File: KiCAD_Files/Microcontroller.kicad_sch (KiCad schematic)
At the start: 33 parts, among them J403 RJE721881411, J404 RJE721881411, U401 OwnTech_SPIN, U402 TCAN334GDR

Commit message: Schematic close to completion.
Signed-off-by: Jean Alinei <jean.alinei@owntech.org>
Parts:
- C40: renamed from C401; LCSC (none) -> C5449000
- renumbered J403 to J12, J404 to J13, JP412 to JP1, JP413 to JP2, JP405 to JP3, JP406 to JP4, JP414 to JP5, JP415 to JP6, JP402 to JP7, JP401 to JP8, R421 to R12, R406 to R13, R407 to R14, R403 to R15, R405 to R16, R402 to R17, R404 to R18, R401 to R19, TH402 to TH1, TH401 to TH2, TP409 to TP1, TP408 to TP10, TP410 to TP2, TP401 to TP3, TP405 to TP4, TP402 to TP5, TP406 to TP6, TP403 to TP7, TP407 to TP8, TP404 to TP9, U401 to U3, U402 to U4

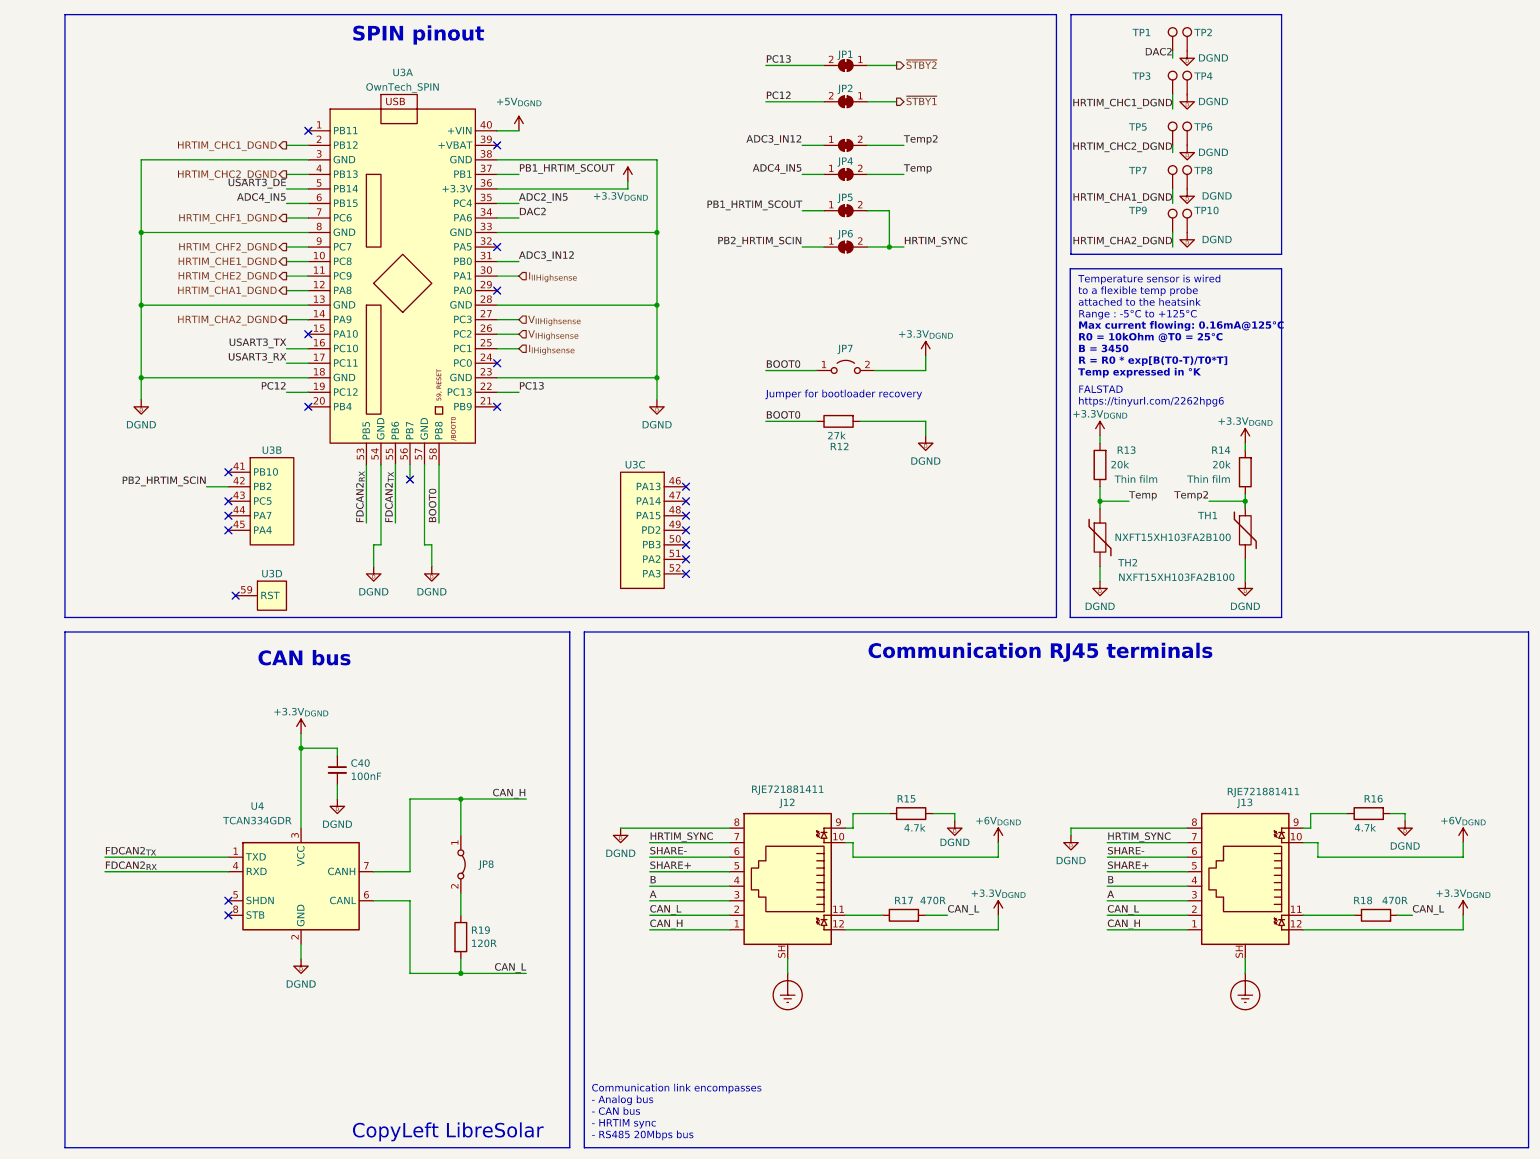
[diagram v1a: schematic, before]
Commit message: First routing pass complete.
Signed-off-by: Jean Alinei <jean.alinei@owntech.org>
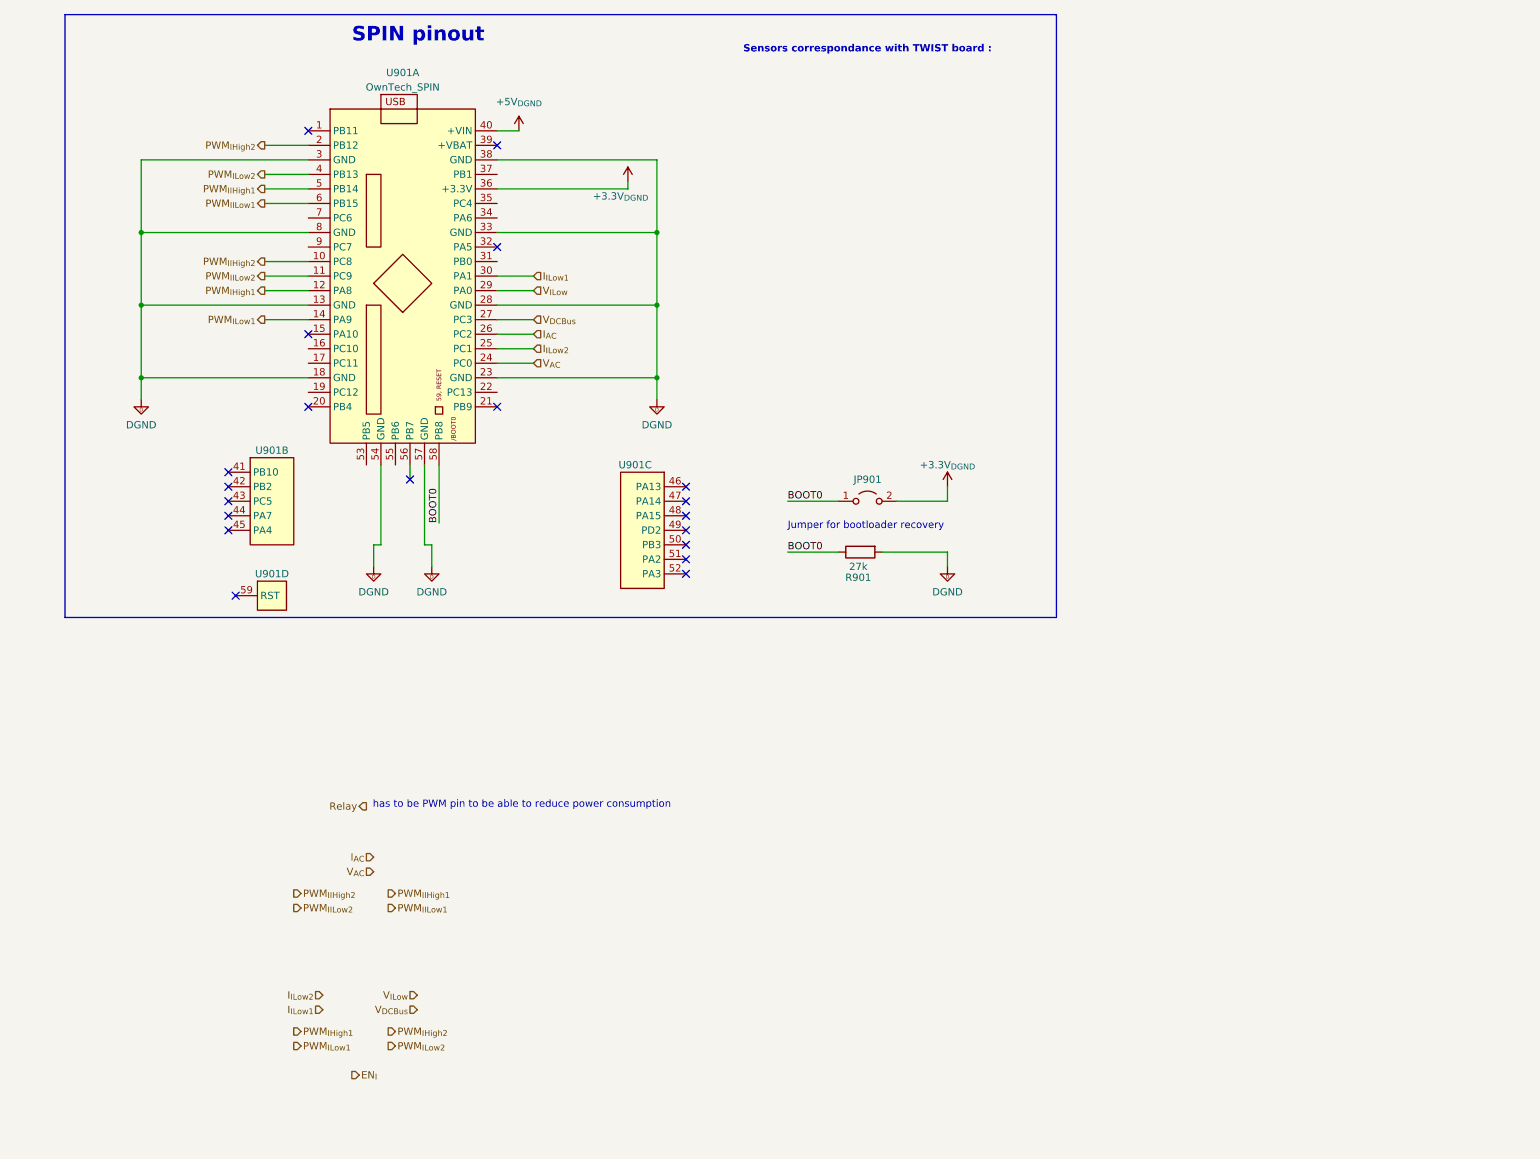
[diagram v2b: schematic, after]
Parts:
- removed C40: 100nF, Capacitor_SMD:C_1206_3216Metric, symbol Device:C_Small
- removed J12, J13: RJE721881411, Footprints:ethernet_RJE721881411, symbol Connector:RJ45_LED_Shielded
- removed JP1, JP2, JP4, JP5, JP6: Jumper_2_Bridged, Jumper:SolderJumper-2_P1.3mm_Bridged_RoundedPad1.0x1.5mm, symbol Jumper:SolderJumper_2_Bridged
- removed JP3: Jumper_2_Bridged, Jumper:SolderJumper-2_P1.3mm_Bridged_Pad1.0x1.5mm, symbol Jumper:SolderJumper_2_Bridged
- removed JP8: Jumper, Connector_PinHeader_2.54mm:PinHeader_1x02_P2.54mm_Vertical, symbol Jumper:Jumper_2_Bridged
- removed R13, R14: 20k, Footprints:R_0805_2012Metric, symbol Device:R
- removed R15, R16: 4.7k, Footprints:R_0805_2012Metric, symbol Device:R
- removed R17, R18: 470R, Footprints:R_0805_2012Metric, symbol Device:R
- removed R19: 120R, Footprints:R_0805_2012Metric, symbol Device:R
- removed TH1, TH2: NXFT15XH103FA2B100, Connector_PinHeader_2.00mm:PinHeader_1x02_P2.00mm_Vertical, symbol Device:Thermistor
- removed TP1, TP10, TP2, TP3, TP4, TP5, TP6, TP7, TP8, TP9: TestPoint, Footprints:TestPoint_THTPad_D1.5mm_Drill0.7mm, symbol Connector:TestPoint
- removed U4: TCAN334GDR, Footprints:SOIC-8_3.9x4.9mm_P1.27mm, symbol Interface_CAN_LIN:TCAN334
- U901: renamed from U3; footprint Footprints:OwnTech_SPINTHT -> Footprints:OwnTech_SPINTHT_1
- renumbered JP7 to JP901, R12 to R901
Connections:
- net V_{AC}: now reaches U901.24 (PC0)
- net V_{ILow}: now reaches U901.29 (PA0)
- net ADC2_IN5: no longer names the net of U901.35 (PC4)
- net ADC3_IN12: no longer names the net of U901.31 (PB0)
- net ADC4_IN5 renamed PWM_{IILow1}
- net DAC2: no longer names the net of U901.34 (PA6)
- net FDCAN2_{RX}: no longer names the net of U901.53 (PB5)
- net FDCAN2_{TX}: no longer names the net of U901.55 (PB6)
- net HRTIM_CHA1_DGND renamed PWM_{IHigh1}
- net HRTIM_CHA2_DGND renamed PWM_{ILow1}
- net HRTIM_CHC1_DGND renamed PWM_{IHigh2}
- net HRTIM_CHC2_DGND renamed PWM_{ILow2}
- net HRTIM_CHE1_DGND renamed PWM_{IIHigh2}
- net HRTIM_CHE2_DGND renamed PWM_{IILow2}
- net HRTIM_CHF1_DGND: no longer names the net of U901.7 (PC6)
- net HRTIM_CHF2_DGND: no longer names the net of U901.9 (PC7)
- net I_{IHighsense} renamed I_{ILow2}
- net I_{IIHighsense} renamed I_{ILow1}
- net PB1_HRTIM_SCOUT: no longer names the net of U901.37 (PB1)
- net PB2_HRTIM_SCIN: no longer names the net of U901.42 (PB2)
- net PC12: no longer names the net of U901.19 (PC12)
- net PC13: no longer names the net of U901.22 (PC13)
- net USART3_DE renamed PWM_{IIHigh1}
- net USART3_RX: no longer names the net of U901.17 (PC11)
- net USART3_TX: no longer names the net of U901.16 (PC10)
- net V_{IHighsense} renamed I_{AC}
- net V_{IIHighsense} renamed V_{DCBus}
- no-connect marks 23 -> 20
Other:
- note added: "Sensors correspondance with TWIST board :"
- note added: "has to be PWM pin to be able to reduce power consumption"
- note removed: "CAN bus"
- note removed: "Communication RJ45 terminals"
- note removed: "Communication link encompasses - Analog bus - CAN bus - HRTIM sync - RS485 20Mbps bus"
- note removed: "CopyLeft LibreSolar"
- note removed: "FALSTAD https://tinyurl.com/2262hpg6"
- note removed: "Max current flowing: 0.16mA@125°C R0 = 10kOhm @T0 = 25°C B = 3450 R = R0 * exp[B(T0-T)/T0*T] Temp expressed in °K"
- note removed: "Temperature sensor is wired to a flexible temp probe attached to the heatsink Range : -5°C to +125°C"
- moved on the sheet: JP901, R901

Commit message: Added missing tracks for sensors and relay. Fixed many routing issues.
Signed-off-by: Jean Alinei <jean.alinei@owntech.org>
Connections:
- net EN_{I}: now also U901.19 (PC12)
- net Relay: now also U901.22 (PC13)
- net DIS_{HV}: now reaches U901.21 (PB9)
- no-connect marks 20 -> 19
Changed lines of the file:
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@@
 	(rectangle
 		(start 23.495 15.24)
-		(end 196.85 120.65)
+		(end 229.87 120.65)
 		(stroke
 			(width 0)
@@
 	)
 	(no_connect
-		(at 99.06 83.82)
-	)
-	(no_connect
 		(at 132.08 105.41)
 	)
@@
 	(wire
 		(pts
+			(xy 99.06 81.28) (xy 105.41 81.28)
+		)
+		(stroke
+			(width 0)
+			(type default)
+		)
+	)
+	(wire
+		(pts
 			(xy 99.06 63.5) (xy 105.41 63.5)
 		)
@@
 	(wire
 		(pts
+			(xy 99.06 83.82) (xy 105.41 83.82)
+		)
+		(stroke
+			(width 0)
+			(type default)
+		)
+	)
+	(wire
+		(pts
 			(xy 58.42 63.5) (xy 66.04 63.5)
 		)
@@
 		(pts
 			(xy 58.42 58.42) (xy 66.04 58.42)
+		)
+		(stroke
+			(width 0)
+			(type default)
+		)
+	)
+	(wire
+		(pts
+			(xy 58.42 81.28) (xy 66.04 81.28)
 		)
 		(stroke
@@
 		)
 		(column_widths 11.43 11.43)
-		(row_heights 5.08 3.302 3.302 3.302 3.302 3.302 3.302 3.302 3.302)
+		(row_heights 5.08 3.302 3.302 3.302 3.302 3.302 3.302 3.302 3.302 3.302)
 		(cells
 			(table_cell "µVerter"
@@
 				(exclude_from_sim no)
 				(at 163.83 80.264 0)
+				(size 11.43 3.302)
+				(margins 0.9525 0.9525 0.9525 0.9525)
+				(span 1 1)
+				(fill
+					(type none)
+				)
+				(effects
+					(font
+						(size 1.27 1.27)
+					)
+					(justify left top)
+				)
+			)
+			(table_cell "Relay"
+				(exclude_from_sim no)
+				(at 152.4 83.566 0)
+				(size 11.43 3.302)
+				(margins 0.9525 0.9525 0.9525 0.9525)
+				(span 1 1)
+				(fill
+					(type none)
+				)
+				(effects
+					(font
+						(size 1.27 1.27)
+					)
+					(justify left top)
+				)
+			)
+			(table_cell "TIM1 CH1n"
+				(exclude_from_sim no)
+				(at 163.83 83.566 0)
 				(size 11.43 3.302)
 				(margins 0.9525 0.9525 0.9525 0.9525)
@@
 		)
 	)
+	(hierarchical_label "Relay"
+		(shape output)
+		(at 105.41 81.28 0)
+		(effects
+			(font
+				(size 1.27 1.27)
+			)
+			(justify left)
+		)
+	)
+	(hierarchical_label "DIS_{HV}"
+		(shape output)
+		(at 105.41 83.82 0)
+		(effects
+			(font
+				(size 1.27 1.27)
+			)
+			(justify left)
+		)
+	)
 	(hierarchical_label "PWM_{ILow1}"
 		(shape output)
@@
 	(hierarchical_label "EN_{I}"
 		(shape output)
+		(at 58.42 81.28 180)
+		(effects
+			(font
+				(size 1.27 1.27)
+			)
+			(justify right)
+		)
+	)
+	(hierarchical_label "EN_{I}"
+		(shape output)
 		(at 73.66 200.66 0)
 		(effects
@@
 		)
 	)
+	(rule_area
+		(polyline
+			(pts
+				(xy 17.78 13.97) (xy 236.22 13.97) (xy 236.22 129.54) (xy 17.78 129.54)
+			)
+			(stroke
+				(width 0)
+				(type dash)
+			)
+			(fill
+				(type none)
+			)
+		)
+	)
+	(netclass_flag ""
+		(length 2.54)
+		(shape round)
+		(at 21.59 129.54 0)
+		(fields_autoplaced yes)
+		(effects
+			(font
+				(size 1.27 1.27)
+			)
+			(justify left bottom)
+		)
+		(property "Netclass" "DGND"
+			(at 22.2885 127 0)
+			(effects
+				(font
+					(size 1.27 1.27)
+				)
+				(justify left)
+			)
+		)
+		(property "Component Class" ""
+			(at -231.14 49.53 0)
+			(effects
+				(font
+					(size 1.27 1.27)
+					(italic yes)
+				)
+			)
+		)
+	)
